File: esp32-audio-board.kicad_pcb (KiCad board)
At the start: 2 copper layers, 60 x 80.5 mm, 120 parts, among them IC1 XC6220A331MR-G, IC2 XC6220A331MR-G, J1 EN_PAD0, J10 PWR_LED+, J11 HP_LOUT1, J12 HP_ROUT1, J13 HP_LOUT2, J14 HP_ROUT2, J15 MIC_LIN1, J16 MIC_LIN1_GND, J17 MIC_RIN1, J18 MIC_RIN1_GND, J19 HP_1GND, J2 Conn_01x02_Pin, J20 HP_2GND, J21 VP_PAD0, J22 PWR_LED-, J23 CHG_LED+, J24 CHG_LED-, J3 USB_C_Receptacle_USB2.0_16P, J4 EN_PAD1, J5 VP_PAD1, J6 VN_PAD0, J7 VN_PAD1, J8 IO14_PAD0, J9 IO14_PAD1, Q1 SS8050, Q2 SS8050, Q4 AO3401A, U1 ESP32-WROOM-32E, U2 CH340C, U3 MCP73831-2-OT, U5 ES8388

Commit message: esp32-audio-board: add ferrite beads on pwr lanes
Added two ferrite beads (BLM) on the high power
rails - from USB-C/battery, to lower the EMI.

Added some little improvements to the schematic and PCB.

Signed-off-by: RaresCon <rares.constantin2002@gmail.com>
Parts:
- added FB1: BLM18SG121TN1D, blm18sg121tn1d:BLM18EG101TH1D, F.Cu at (203.0, 130.7)
- added FB2: BLM18SG121TN1D, blm18sg121tn1d:BLM18EG101TH1D, F.Cu at (197.5, 117.7)
- moved R26 5.28 mm to (226.5, 97.9), turned to -90 degrees
- moved C35 5.26 mm to (225.9, 100.5)
- moved C33 3.05 mm to (220.4, 100.5)
- moved R24 2.65 mm to (221.3, 97.9), turned to -90 degrees
- moved C34 2.17 mm to (223.2, 100.5)
- moved R25 2.14 mm to (223.8, 97.9), turned to -90 degrees
- moved U5 1.91 mm to (219.6, 109.7)
- moved U1 0.30 mm to (216.5, 82.9)
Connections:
- net Net-(U2-UD+) renamed /D+
- net Net-(U2-UD-) renamed /D-
- C10 pad 1: VBAT -> Net-(IC2-CE)
- C11 pad 1: VI -> Net-(IC1-CE)
- C14 pad 1: VBAT -> Net-(IC2-CE)
- C7 pad 1: VI -> Net-(IC1-CE)
- IC1 pad 1: VI -> Net-(IC1-CE)
- IC1 pad 3: VI -> Net-(IC1-CE)
- IC2 pad 1: VBAT -> Net-(IC2-CE)
- IC2 pad 3: VBAT -> Net-(IC2-CE)

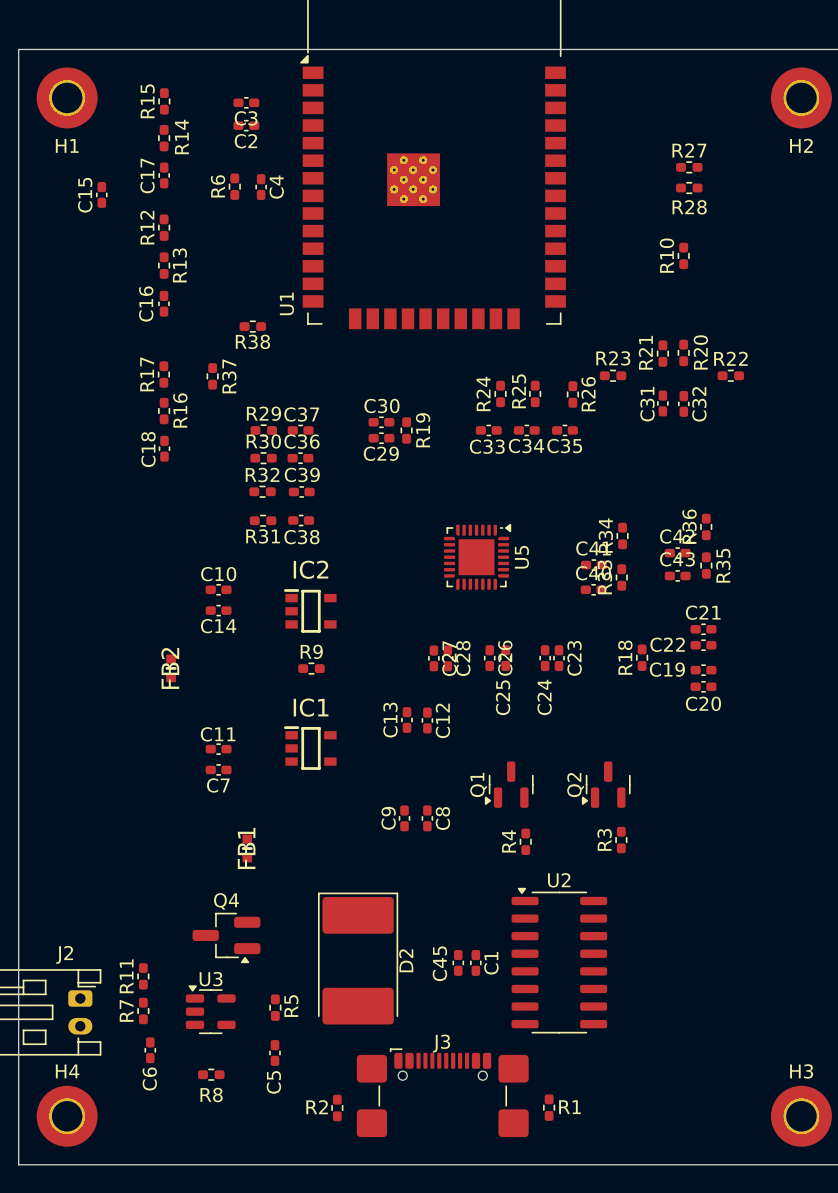
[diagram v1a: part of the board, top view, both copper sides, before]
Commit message: esp32-audio-board: rehook ES8388
Rehooked the ES8388 to allow the routing to be
easier and allow ground planes under the I2C and
I2S to limit EMI and noise.

Signed-off-by: RaresCon <rares.constantin2002@gmail.com>
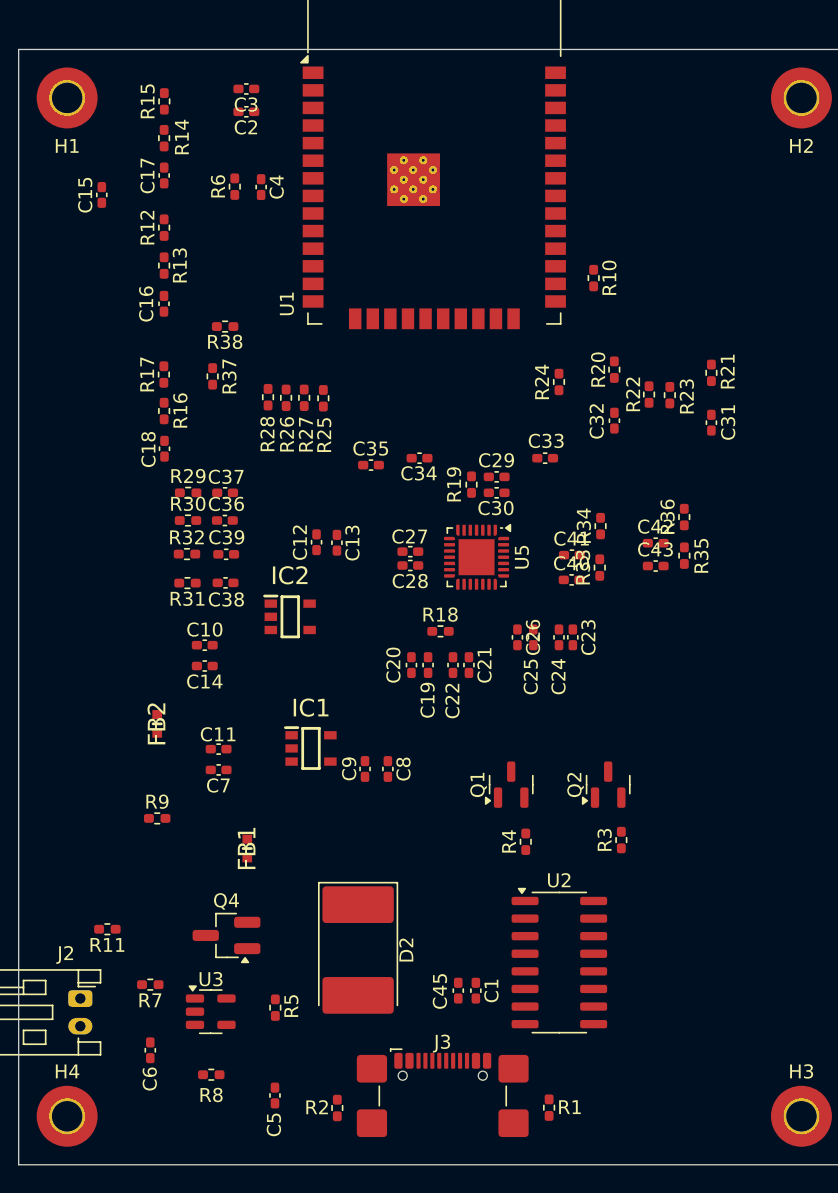
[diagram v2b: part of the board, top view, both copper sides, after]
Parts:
- J8: value IO14_PAD0 -> IO34_PAD0
- J9: value IO14_PAD1 -> IO34_PAD1
- moved R28 33.9 mm to (204.5, 98.1), turned to -90 degrees
- moved R27 32.4 mm to (207.1, 98.1), turned to -90 degrees
- moved C20 21.1 mm to (214.8, 117.4), turned to -90 degrees
- moved R26 20.7 mm to (205.8, 98.1)
- moved C19 19.9 mm to (216.1, 117.4), turned to -90 degrees
- moved C22 18.1 mm to (217.8, 117.4), turned to -90 degrees
- moved C21 17.1 mm to (219.0, 117.4), turned to -90 degrees
- moved R9 15.5 mm to (196.5, 128.5)
- moved R25 15.3 mm to (208.5, 98.2)
- moved C12 15.1 mm to (208.0, 108.6), turned to 90 degrees
- moved R18 14.7 mm to (216.9, 115.0), turned to 180 degrees
- moved C35 14.2 mm to (211.9, 103.0), turned to 0 degrees
- moved C13 13.8 mm to (209.5, 108.6), turned to 90 degrees
- moved C30 9.75 mm to (221.0, 105.0), turned to 0 degrees
- moved C29 8.77 mm to (221.0, 103.8), turned to 0 degrees
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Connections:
- J2 pad 1: GND -> VBAT
- J2 pad 2: VBAT -> GND
- R16 pad 1: ESP_IO14 -> ESP_IO34
- R17 pad 1: ESP_IO14 -> ESP_IO34
- U1 pad 11: unconnected-(U1-IO26-Pad11) -> DATA_IN
- U1 pad 12: unconnected-(U1-IO27-Pad12) -> WS
- U1 pad 13: ESP_IO14 -> DATA_OUT
- U1 pad 16: unconnected-(U1-IO13-Pad16) -> BCK
- U1 pad 29: BCK -> unconnected-(U1-IO5-Pad29)
- U1 pad 30: WS -> SCL
- U1 pad 31: DATA_IN -> SDA
- U1 pad 33: DATA_OUT -> unconnected-(U1-IO21-Pad33)
- U1 pad 36: SDA -> unconnected-(U1-IO22-Pad36)
- U1 pad 37: SCL -> unconnected-(U1-IO23-Pad37)
- U1 pad 6: BAT_LVL -> ESP_IO34
- U1 pad 7: unconnected-(U1-IO35-Pad7) -> BAT_LVL
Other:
- copper layers 2 -> 4

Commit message: esp32-audio-board: route initial power
Added routing for the USB-C and battery initial
lanes/traces to also see how small the PCB can
be as width.

Signed-off-by: RaresCon <rares.constantin2002@gmail.com>
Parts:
- added D1: ESDA5V3SC5, Package_TO_SOT_SMD:SOT-23-5_HandSoldering, F.Cu at (230.5, 142.5)
- J3: footprint Connector_USB:USB_C_Receptacle_GCT_USB4110 -> Connector_USB:USB_C_Receptacle_GCT_USB4105-xx-A_16P_TopMnt_Horizontal
- moved J23 60.5 mm to (203.5, 148.0)
- moved J24 56.2 mm to (203.5, 151.0), turned to 180 degrees
- moved R11 16.1 mm to (205.6, 146.4), turned to -90 degrees
- moved IC1 8.50 mm to (211.5, 131.0)
- moved R8 8.12 mm to (208.5, 146.4), turned to 90 degrees
- moved C6 6.96 mm to (199.9, 139.5), turned to 180 degrees
- moved R3 5.00 mm to (225.0, 130.0)
- moved R7 4.77 mm to (200.7, 141.4), turned to -90 degrees
- moved C1 4.33 mm to (215.2, 141.5)
- moved U2 4.19 mm to (222.0, 136.6), turned to 180 degrees
- moved Q2 4.10 mm to (224.9, 126.1)
- moved U3 3.69 mm to (203.5, 140.5), turned to -90 degrees
- moved Q4 3.15 mm to (204.5, 136.0)
- moved C5 3.00 mm to (207.1, 146.4)
- moved C8 2.95 mm to (213.5, 122.0)
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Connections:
- R4 pad 1: Serial-RTS -> Net-(Q2-B)
- R4 pad 2: Net-(Q2-B) -> Serial-RTS
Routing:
- net Serial-RX: track 0.00 -> 69.4 mm, vias 0 -> 2
- net Serial-TX: track 0.00 -> 65.2 mm, vias 0 -> 2
- net VBUS: track 0.00 -> 51.6 mm
- net +3V3: track 0.00 -> 28.6 mm, vias 0 -> 2
- net /D-: track 0.00 -> 27.7 mm
- net /D+: track 0.00 -> 25.9 mm
- net Serial-RTS: track 0.00 -> 22.3 mm
- net VBAT: track 0.00 -> 18.1 mm
- net Serial-DTR: track 0.00 -> 13.8 mm
- net Net-(IC1-CE): track 0.00 -> 10.3 mm
- net Net-(Q1-B): track 0.00 -> 8.80 mm
- net VI: track 0.00 -> 8.61 mm
- net Net-(J3-CC2): track 0.00 -> 6.98 mm
- net Net-(J3-CC1): track 0.00 -> 6.83 mm
- net Net-(U3-STAT): track 0.00 -> 4.76 mm
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- added copper zone on B.Cu, net GND
- added copper zone on F.Cu, net GND
- added copper zone on In1.Cu, net GND
- added copper zone on In2.Cu, net VBAT

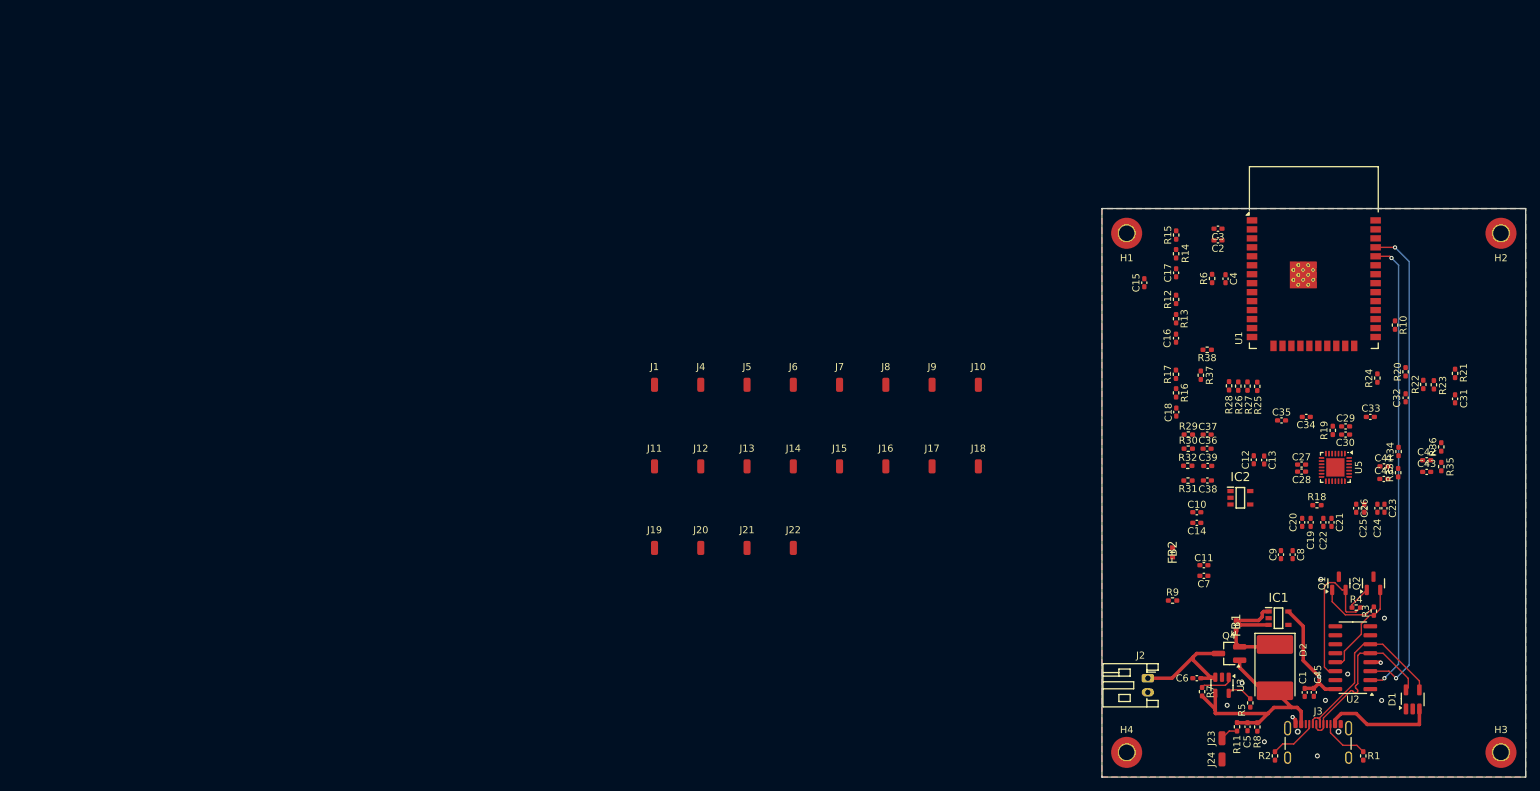
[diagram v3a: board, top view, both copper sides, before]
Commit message: esp32-audio-board: complete PCB general design
Added the initial PCB complete design.

Changed the CH340C with CP2102 to allow the board to
consume less energy while not connected to USB.

Signed-off-by: RaresCon <rares.constantin2002@gmail.com>
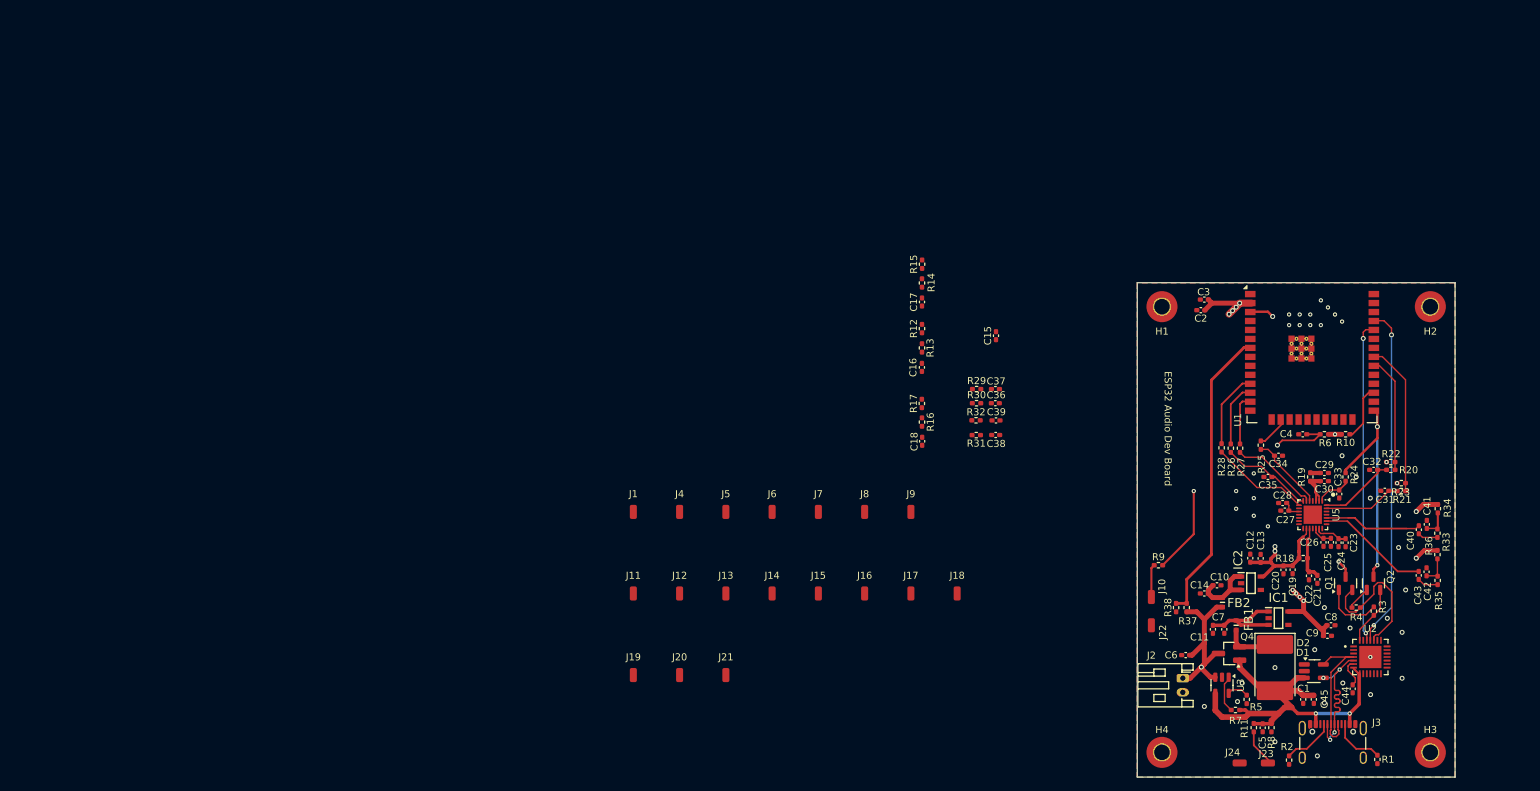
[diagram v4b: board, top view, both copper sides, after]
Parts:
- added C44: 0.1uF, Capacitor_SMD:C_0402_1005Metric_Pad0.74x0.62mm_HandSolder, F.Cu at (222.0, 141.0)
- U1: footprint RF_Module:ESP32-WROOM-32D -> RF_Module:ESP32-WROOM-32E
- U2: value CH340C -> CP2102; footprint Package_SO:SOIC-16_3.9x9.9mm_P1.27mm -> cp2102:QFN50P500X500X100-29N
- moved J22 51.9 mm to (193.5, 132.0)
- moved J10 38.8 mm to (193.5, 128.0)
- moved R38 36.8 mm to (197.0, 129.5), turned to -90 degrees
- moved C16 36.2 mm to (161.0, 95.5)
- moved C17 36.2 mm to (161.0, 86.2)
- moved C18 36.2 mm to (161.0, 106.0)
- moved R12 36.2 mm to (161.0, 90.0)
- moved R13 36.2 mm to (161.0, 92.7)
- moved R14 36.2 mm to (161.0, 83.5)
- moved R15 36.2 mm to (161.0, 80.9)
- moved R16 36.2 mm to (161.0, 103.2)
- moved R17 36.2 mm to (161.0, 100.6)
- moved R37 33.0 mm to (198.5, 129.5)
- moved C36 30.7 mm to (171.4, 100.6)
- moved R32 30.7 mm to (168.7, 103.0)
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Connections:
- C1 pad 1: +3V3 -> VBUS
- C45 pad 1: +3V3 -> VBUS
- U2 pad 1: GND -> unconnected-(U2-DCD-Pad1)
- U2 pad 13: Serial-DTR -> unconnected-(U2-NC-Pad10)_5
- U2 pad 14: Serial-RTS -> unconnected-(U2-NC-Pad10)_4
- U2 pad 16: +3V3 -> unconnected-(U2-NC-Pad10)_6
- U2 pad 2: Serial-TX -> unconnected-(U2-RI-Pad2)
- U2 pad 3: Serial-RX -> GND
- U2 pad 4: +3V3 -> /D+
- U2 pad 5: /D+ -> /D-
- U2 pad 6: /D- -> Net-(U2-VDD)
- U2 pad 7: unconnected-(U2-NC-Pad7) -> VBUS
- U2 pad 8: unconnected-(U2-NC-Pad8) -> VBUS
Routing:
- net +3V3: track 28.6 -> 116.8 mm, vias 2 -> 10
- net +3V3 Audio: track 0.00 -> 79.9 mm, vias 0 -> 6
- net ESP-EN: track 0.00 -> 53.0 mm, vias 0 -> 3
- net BAT_LVL: track 0.00 -> 42.2 mm
- net ESP-IO0: track 0.00 -> 32.3 mm, vias 0 -> 2
- net SDA: track 0.00 -> 21.4 mm
- net Serial-RX: track 69.4 -> 48.1 mm
- net Serial-TX: track 65.2 -> 45.7 mm
- net SCL: track 0.00 -> 16.2 mm
- net ES8388_RIN1: track 0.00 -> 16.0 mm
- net Net-(U5-ASDOUT): track 0.00 -> 14.1 mm
- net ES8388_LIN1: track 0.00 -> 13.9 mm
- net ES8388_LRCK: track 0.00 -> 13.1 mm
- net Net-(U5-DSDIN): track 0.00 -> 12.5 mm
- net DATA_IN: track 0.00 -> 11.1 mm
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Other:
- board size 60 x 80.5 mm -> 45 x 70 mm
- board text added: "ESP32 Audio Dev Board"
